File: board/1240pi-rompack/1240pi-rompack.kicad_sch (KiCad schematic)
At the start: 2 parts, among them P1 CardEdge_ROMPACK

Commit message: Update board license to CERN-OHL-S v2+.
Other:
- company: (none) -> © 2022 Sam Hanes, licensed under CERN-OHL-S v2+
- title: (none) -> 1240-Pi ROM Pack

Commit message: Add more stuff to rompack board.
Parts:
- removed unit 2 of A1
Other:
- added sheet CM4 Direct IO (cm4_io.kicad_sch)

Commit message: Add buffers to card-edge connector.
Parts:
- removed P1: CardEdge_ROMPACK, 0Local:CardEdge_18x2, symbol 0Local:CardEdge_ROMPACK
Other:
- added sheet Control Proc Interface (host_conp.kicad_sch)

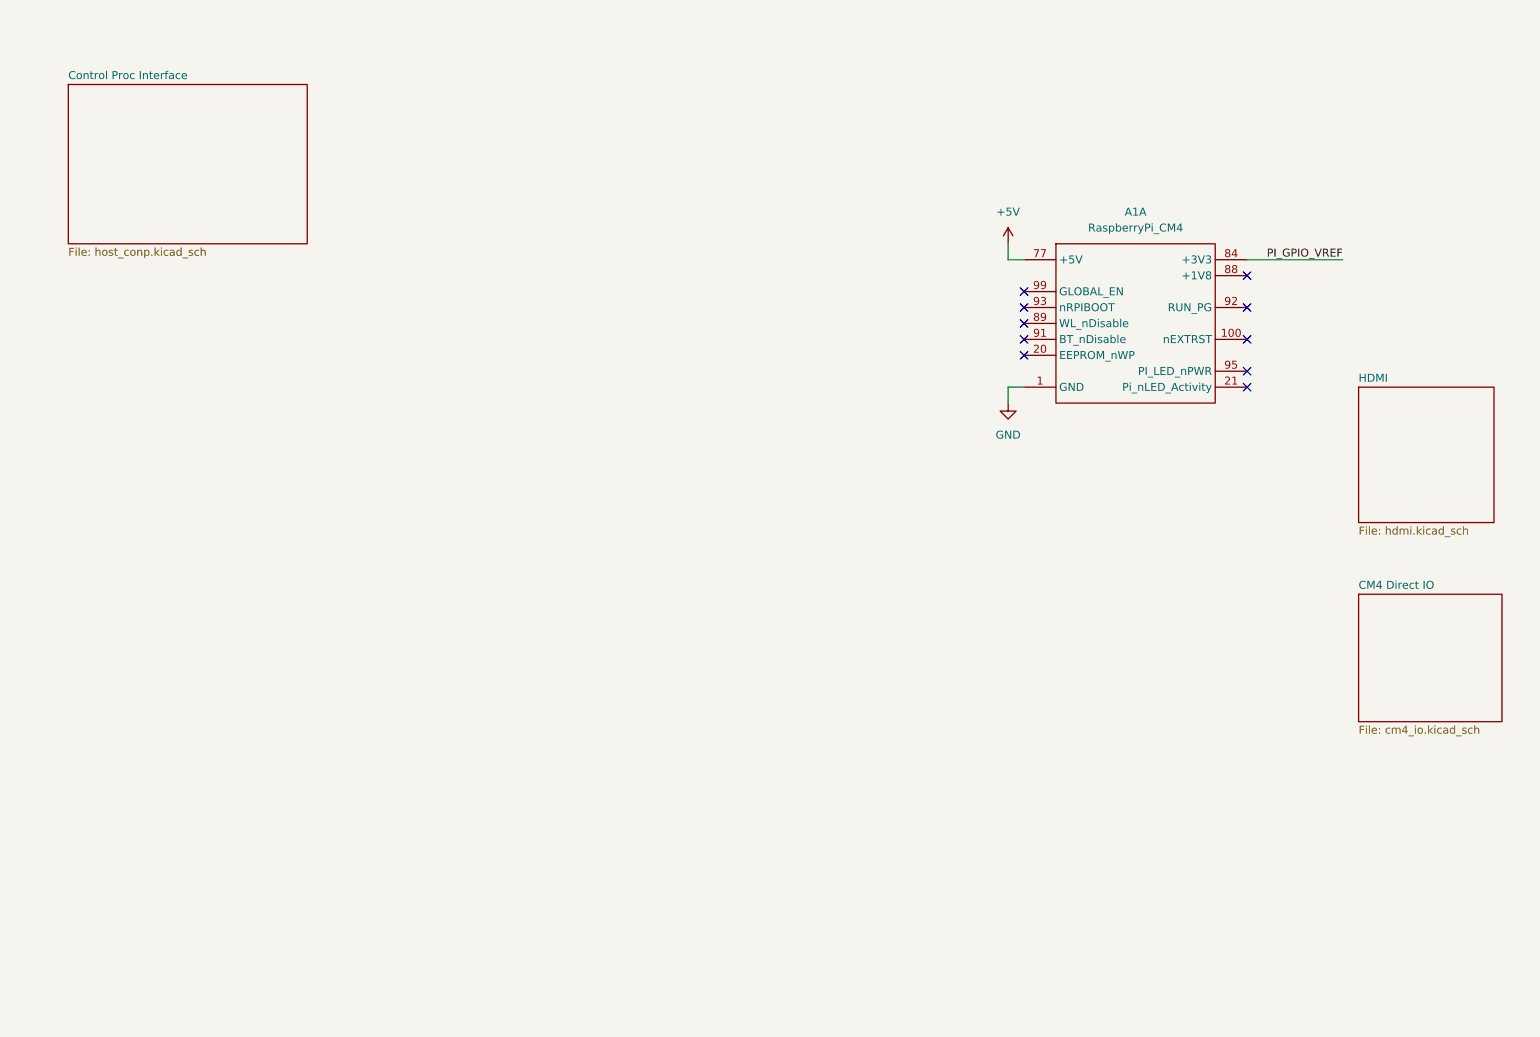
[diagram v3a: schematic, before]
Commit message: Split connectors out of CM4 footprint.
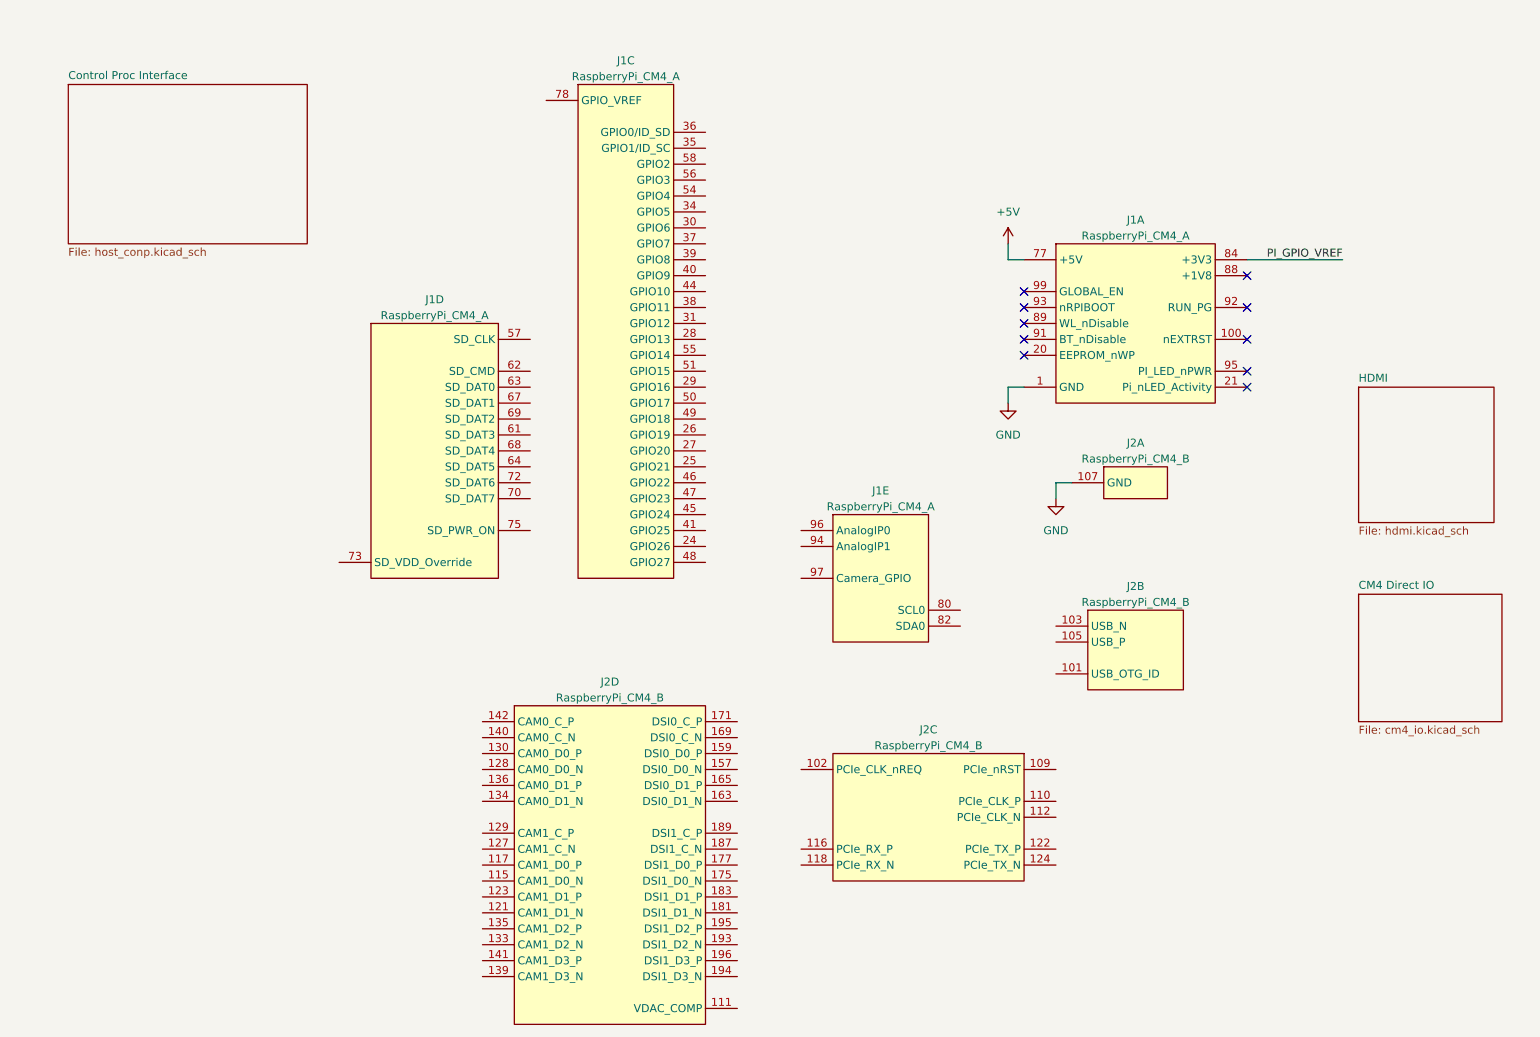
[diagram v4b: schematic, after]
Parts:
- removed A1: RaspberryPi_CM4, 0Local:RaspberryPi_CM4, symbol 0Local:RaspberryPi_CM4
- added J1: RaspberryPi_CM4_A, 0Local:Hirose_DF40C-100DS-0.4V, symbol 0Local:RaspberryPi_CM4_A
- added J2: RaspberryPi_CM4_B, 0Local:Hirose_DF40C-100DS-0.4V, symbol 0Local:RaspberryPi_CM4_B
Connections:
- net +5V: now also J1.77 (+5V), J1.79 (+5V), J1.81 (+5V), J1.83 (+5V), J1.85 (+5V), J1.87 (+5V)
- net GND: now also J1.1 (GND), J1.13 (GND), J1.14 (GND), J1.2 (GND), J1.22 (GND), J1.23 (GND), J1.32 (GND), J1.33 (GND), J1.42 (GND), J1.43 (GND), J1.52 (GND), J1.53 (GND), J1.59 (GND), J1.60 (GND), J1.65 (GND), J1.66 (GND), J1.7 (GND), J1.71 (GND), J1.74 (GND), J1.8 (GND), J1.98 (GND), J2.107 (GND), J2.108 (GND), J2.113 (GND), J2.114 (GND), J2.119 (GND), J2.120 (GND), J2.125 (GND), J2.126 (GND), J2.131 (GND), J2.132 (GND), J2.137 (GND), J2.138 (GND), J2.144 (GND), J2.150 (GND), J2.155 (GND), J2.156 (GND), J2.161 (GND), J2.162 (GND), J2.167 (GND), J2.168 (GND), J2.173 (GND), J2.174 (GND), J2.179 (GND), J2.180 (GND), J2.185 (GND), J2.186 (GND), J2.191 (GND), J2.192 (GND), J2.197 (GND), J2.198 (GND)
- net PI_GPIO_VREF: now also J1.84 (+3V3), J1.86 (+3V3)
- new net: J2.104 (Reserved), J2.106 (Reserved)
- new net: J1.88 (+1V8), J1.90 (+1V8)

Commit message: Route HDMI output port.
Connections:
- net PI_GPIO_VREF is gone; now on net +3V3_PI: J1.84 (+3V3), J1.86 (+3V3)
- net GND: now also J2.13 (GND), J2.14 (GND), J2.19 (GND), J2.20 (GND), J2.25 (GND), J2.26 (GND), J2.31 (GND), J2.32 (GND), J2.37 (GND), J2.38 (GND), J2.44 (GND), J2.50 (GND), J2.55 (GND), J2.56 (GND), J2.61 (GND), J2.62 (GND), J2.67 (GND), J2.68 (GND), J2.7 (GND), J2.73 (GND), J2.74 (GND), J2.79 (GND), J2.8 (GND), J2.80 (GND), J2.85 (GND), J2.86 (GND), J2.91 (GND), J2.92 (GND), J2.97 (GND), J2.98 (GND); no longer J2.107 (GND), J2.108 (GND), J2.113 (GND), J2.114 (GND), J2.119 (GND), J2.120 (GND), J2.125 (GND), J2.126 (GND), J2.131 (GND), J2.132 (GND), J2.137 (GND), J2.138 (GND), J2.144 (GND), J2.150 (GND), J2.155 (GND), J2.156 (GND), J2.161 (GND), J2.162 (GND), J2.167 (GND), J2.168 (GND), J2.173 (GND), J2.174 (GND), J2.179 (GND), J2.180 (GND), J2.185 (GND), J2.186 (GND), J2.191 (GND), J2.192 (GND), J2.197 (GND), J2.198 (GND)
- net +3V3_PI: now reaches J1.78 (GPIO_VREF)
- new net: J2.4 (Reserved), J2.6 (Reserved)
- no-connect marks 10 -> 50

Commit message: Rearrange IO Proc hat, add IO Proc interface.
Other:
- added sheet IO Proc Interface (host_iop.kicad_sch)
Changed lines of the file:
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@@
     (pin "97")
+  )
+  (sheet (at 25.4 63.5) (size 38.1 17.78) (fields_autoplaced)
+    (stroke (width 0.1524) (type solid) (color 0 0 0 0))
+    (fill (color 0 0 0 0.0000))
+    (property "Sheet name" "IO Proc Interface" (id 0) (at 25.4 62.7884 0)
+      (effects (font (size 1.27 1.27)) (justify left bottom))
+    )
+    (property "Sheet file" "host_iop.kicad_sch" (id 1) (at 25.4 81.8646 0)
+      (effects (font (size 1.27 1.27)) (justify left top))
+    )
   )
   (sheet (at 231.14 73.66) (size 21.59 21.59) (fields_autoplaced)
@@
     (path "/557d6630-372d-4085-9364-bb77b12a009c" (page "3"))
     (path "/8e577e1a-6946-4ecf-bc7a-64c4753e6a83" (page "4"))
+    (path "/0ec83c48-0d15-4cb4-b67d-a472cab6ad18" (page "5"))
   )
   (symbol_instances
@@
       (reference "#PWR015") (unit 1) (value "GND") (footprint "")
     )
+    (path "/0ec83c48-0d15-4cb4-b67d-a472cab6ad18/93ac004d-c024-45a1-8a2d-8dc7a55e2075"
+      (reference "#PWR016") (unit 1) (value "GND") (footprint "")
+    )
+    (path "/0ec83c48-0d15-4cb4-b67d-a472cab6ad18/0b7be37d-e9f8-444e-81d8-2ecd5de94269"
+      (reference "#PWR018") (unit 1) (value "+3V3") (footprint "")
+    )
+    (path "/0ec83c48-0d15-4cb4-b67d-a472cab6ad18/4d0e7104-d065-42c2-b765-992a97fa01f9"
+      (reference "#PWR019") (unit 1) (value "GND") (footprint "")
+    )
+    (path "/0ec83c48-0d15-4cb4-b67d-a472cab6ad18/9472583d-7f0c-4907-bbe6-a33ebae71c80"
+      (reference "#PWR020") (unit 1) (value "+3V3") (footprint "")
+    )
+    (path "/0ec83c48-0d15-4cb4-b67d-a472cab6ad18/992ccc9a-50d2-40ef-8523-82d5fcb8a5b5"
+      (reference "#PWR021") (unit 1) (value "GND") (footprint "")
+    )
+    (path "/0ec83c48-0d15-4cb4-b67d-a472cab6ad18/12dc0334-8f57-4781-88fd-ccad353486d7"
+      (reference "#PWR023") (unit 1) (value "+3V3") (footprint "")
+    )
+    (path "/0ec83c48-0d15-4cb4-b67d-a472cab6ad18/bf24c33c-61d0-4283-b883-cc11b9b471ef"
+      (reference "#PWR024") (unit 1) (value "GND") (footprint "")
+    )
+    (path "/0ec83c48-0d15-4cb4-b67d-a472cab6ad18/40c6d6ce-b70e-48d8-88af-0797aa74ae95"
+      (reference "#PWR025") (unit 1) (value "+3V3") (footprint "")
+    )
+    (path "/0ec83c48-0d15-4cb4-b67d-a472cab6ad18/6183ae4e-3e04-4309-bbb2-5548607b8d9f"
+      (reference "#PWR026") (unit 1) (value "GND") (footprint "")
+    )
+    (path "/0ec83c48-0d15-4cb4-b67d-a472cab6ad18/fe07910f-7cd6-4075-a53e-4994c8a10c97"
+      (reference "#PWR027") (unit 1) (value "+3V3") (footprint "")
+    )
+    (path "/0ec83c48-0d15-4cb4-b67d-a472cab6ad18/49819f16-c8cf-4165-9024-c67944707734"
+      (reference "#PWR028") (unit 1) (value "GND") (footprint "")
+    )
+    (path "/0ec83c48-0d15-4cb4-b67d-a472cab6ad18/7a856fe6-fac2-4cc8-9527-83f0a3fd4ef6"
+      (reference "#PWR029") (unit 1) (value "+3V3") (footprint "")
+    )
+    (path "/0ec83c48-0d15-4cb4-b67d-a472cab6ad18/6fe9e8a5-bf83-48a8-8707-961535626d6d"
+      (reference "#PWR030") (unit 1) (value "GND") (footprint "")
+    )
+    (path "/0ec83c48-0d15-4cb4-b67d-a472cab6ad18/65fc8028-1ea4-4555-b711-62b8fdd258bd"
+      (reference "#PWR031") (unit 1) (value "+3V3") (footprint "")
+    )
+    (path "/0ec83c48-0d15-4cb4-b67d-a472cab6ad18/2dc2dd68-3d0d-4d8e-8775-2ead753ba860"
+      (reference "#PWR032") (unit 1) (value "+3V3") (footprint "")
+    )
+    (path "/0ec83c48-0d15-4cb4-b67d-a472cab6ad18/34621112-d3c2-4e15-93bc-10660c6f30ff"
+      (reference "#PWR033") (unit 1) (value "GND") (footprint "")
+    )
+    (path "/0ec83c48-0d15-4cb4-b67d-a472cab6ad18/93b0fb2f-6762-4d11-9da5-c628a2c19327"
+      (reference "#PWR034") (unit 1) (value "+3V3") (footprint "")
+    )
+    (path "/0ec83c48-0d15-4cb4-b67d-a472cab6ad18/6cc2c5f6-cb49-4ede-8254-fad03fb6778b"
+      (reference "#PWR035") (unit 1) (value "GND") (footprint "")
+    )
     (path "/8e577e1a-6946-4ecf-bc7a-64c4753e6a83/d50c283a-5a7f-4d11-9497-940745422978"
       (reference "#PWR0101") (unit 1) (value "+5V") (footprint "")
@@
       (reference "C4") (unit 1) (value "100n") (footprint "Resistor_SMD:R_0402_1005Metric")
     )
+    (path "/0ec83c48-0d15-4cb4-b67d-a472cab6ad18/9ea09634-f972-492a-bf25-eaf201b36e0a"
+      (reference "C5") (unit 1) (value "100n") (footprint "Resistor_SMD:R_0402_1005Metric")
+    )
+    (path "/0ec83c48-0d15-4cb4-b67d-a472cab6ad18/03dff2aa-49b8-4bb4-8f9f-ad1fb9215e11"
+      (reference "C6") (unit 1) (value "100n") (footprint "Resistor_SMD:R_0402_1005Metric")
+    )
+    (path "/0ec83c48-0d15-4cb4-b67d-a472cab6ad18/8721a204-5411-4299-bda0-1043e3da5b1e"
+      (reference "C7") (unit 1) (value "100n") (footprint "Resistor_SMD:R_0402_1005Metric")
+    )
+    (path "/0ec83c48-0d15-4cb4-b67d-a472cab6ad18/7883bc19-461a-4b15-a93e-b4647bfc69b2"
+      (reference "C8") (unit 1) (value "100n") (footprint "Resistor_SMD:R_0402_1005Metric")
+    )
     (path "/f5a6d0fb-5b44-4044-b2b2-e5b22bf1c0fe"
       (reference "J1") (unit 1) (value "RaspberryPi_CM4_A") (footprint "0Local:Hirose_DF40C-100DS-0.4V")
@@
       (reference "J5") (unit 1) (value "Abracon_ARJM11D7-502-AB-EW2") (footprint "0Local:Abracon_ARJM11D7-502-AB-EW2")
     )
+    (path "/0ec83c48-0d15-4cb4-b67d-a472cab6ad18/a8ed1111-3c7a-43ef-9cf3-39ebe3d6585a"
+      (reference "J6") (unit 1) (value "62684-50210") (footprint "0Local:Amphenol_62684-50210")
+    )
     (path "/8e577e1a-6946-4ecf-bc7a-64c4753e6a83/3c5d25cf-e28f-4124-a0b6-a53705a95120"
       (reference "P1") (unit 1) (value "CardEdge_ROMPACK") (footprint "0Local:CardEdge_18x2")
@@
       (reference "U4") (unit 1) (value "74LVC245A") (footprint "0Local:Nexperia_SOT764-1")
     )
-  )
+    (path "/0ec83c48-0d15-4cb4-b67d-a472cab6ad18/88d2738a-ff98-4de5-a77a-56b51ffe229b"
+      (reference "U5") (unit 1) (value "74LVC245A") (footprint "0Local:Nexperia_SOT764-1")
+    )
+    (path "/0ec83c48-0d15-4cb4-b67d-a472cab6ad18/aea2c5ed-90d8-432c-a6bf-96b42bf41d08"
+      (reference "U6") (unit 1) (value "74LVC245A") (footprint "0Local:Nexperia_SOT764-1")
+    )
+    (path "/0ec83c48-0d15-4cb4-b67d-a472cab6ad18/1a16f8ec-2241-4440-8ca6-5a6115803666"
+      (reference "U7") (unit 1) (value "74LVC245A") (footprint "0Local:Nexperia_SOT764-1")
+    )
+    (path "/0ec83c48-0d15-4cb4-b67d-a472cab6ad18/21371852-a930-42dd-83bc-d02013394216"
+      (reference "U8") (unit 1) (value "74LVC245A") (footprint "0Local:Nexperia_SOT764-1")
+    )
+  )

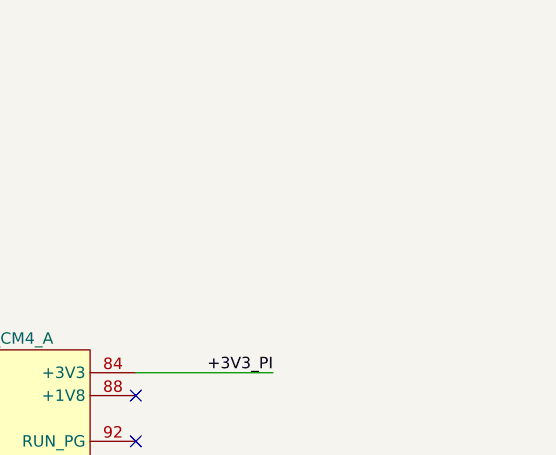
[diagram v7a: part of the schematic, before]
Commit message: Reroute IO Proc hat again and add buffers on rompack board.
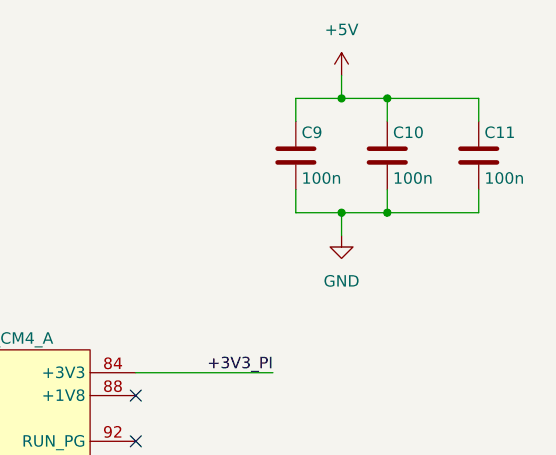
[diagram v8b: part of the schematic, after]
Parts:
- added C10, C11, C9: 100n, Capacitor_SMD:C_0603_1608Metric, symbol Device:C
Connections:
- net +5V: now also C10.1, C11.1, C9.1
- net GND: now also C10.2, C11.2, C9.2
